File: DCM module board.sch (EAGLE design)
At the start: 2 parts

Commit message: Add files via upload
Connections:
- new net N$1: U$1.+IN
- new net N$3: U$1.-IN
- new net N$4: U$2.+IN
- new net N$5: U$2.-IN
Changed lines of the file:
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@@
 <setting verticaltext="up"/>
 </settings>
-<grid distance="0.1" unitdist="inch" unit="inch" style="lines" multiple="1" display="no" altdistance="0.01" altunitdist="inch" altunit="inch"/>
+<grid distance="1" unitdist="mm" unit="mm" style="lines" multiple="1" display="yes" altdistance="0.01" altunitdist="inch" altunit="mm"/>
 <layers>
 <layer number="1" name="Top" color="4" fill="1" visible="no" active="no"/>
@@
 </plain>
 <instances>
-<instance part="U$1" gate="G$1" x="-27.94" y="0" smashed="yes"/>
-<instance part="U$2" gate="G$1" x="48.26" y="0" smashed="yes"/>
+<instance part="U$1" gate="G$1" x="18.36" y="16.02" smashed="yes"/>
+<instance part="U$2" gate="G$1" x="18.36" y="-22.08" smashed="yes"/>
 </instances>
 <busses>
 </busses>
 <nets>
+<net name="N$1" class="0">
+<segment>
+<pinref part="U$1" gate="G$1" pin="+IN"/>
+<wire x1="-4.83" y1="24.02" x2="-15" y2="24.02" width="0.1524" layer="91"/>
+<wire x1="-15" y1="24.02" x2="-15" y2="24" width="0.1524" layer="91"/>
+</segment>
+</net>
+<net name="N$2" class="0">
+<segment>
+<wire x1="-44" y1="25" x2="-64" y2="25" width="0.1524" layer="91"/>
+</segment>
+</net>
+<net name="N$3" class="0">
+<segment>
+<pinref part="U$1" gate="G$1" pin="-IN"/>
+<wire x1="-4.83" y1="8.02" x2="-15" y2="8.02" width="0.1524" layer="91"/>
+<wire x1="-15" y1="8.02" x2="-15" y2="12" width="0.1524" layer="91"/>
+</segment>
+</net>
+<net name="N$4" class="0">
+<segment>
+<wire x1="-15" y1="8" x2="-48" y2="8" width="0.1524" layer="91"/>
+<wire x1="-48" y1="8" x2="-48" y2="-3" width="0.1524" layer="91"/>
+<pinref part="U$2" gate="G$1" pin="+IN"/>
+<wire x1="-48" y1="-3" x2="-48" y2="-14.08" width="0.1524" layer="91"/>
+<wire x1="-48" y1="-14.08" x2="-4.83" y2="-14.08" width="0.1524" layer="91"/>
+<wire x1="-48" y1="-3" x2="-63" y2="-3" width="0.1524" layer="91"/>
+<junction x="-48" y="-3"/>
+</segment>
+</net>
+<net name="N$5" class="0">
+<segment>
+<pinref part="U$2" gate="G$1" pin="-IN"/>
+<wire x1="-4.83" y1="-30.08" x2="-62" y2="-30.08" width="0.1524" layer="91"/>
+<wire x1="-62" y1="-30.08" x2="-62" y2="-30" width="0.1524" layer="91"/>
+</segment>
+</net>
 </nets>
 </sheet>

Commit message: Add files via upload
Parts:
- added C1, C2: (no value), capacitor-emi:B58035U5305M062
- added R1, R2: (no value), resistor-power:RMG100-H
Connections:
- removed net N$4: U$2.+IN
- new net N$2: C2.2, R2.2, U$2.+IN
- new net N$6: U$1.-OUT1, U$1.-OUT2, U$2.-OUT1, U$2.-OUT2
- new net N$7: R1.1
- new net N$8: U$1.+OUT1, U$1.+OUT2, U$2.+OUT1, U$2.+OUT2
- net N$1: now also C1.2, R1.2
- net N$3: now also C2.1, U$2.-IN; no longer U$1.-IN
- net N$5: now also C1.1, R2.1, U$1.-IN; no longer U$2.-IN
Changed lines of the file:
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@@
 <setting verticaltext="up"/>
 </settings>
-<grid distance="1" unitdist="mm" unit="mm" style="lines" multiple="1" display="yes" altdistance="0.01" altunitdist="inch" altunit="mm"/>
+<grid distance="1" unitdist="mm" unit="mm" style="lines" multiple="1" display="yes" altdistance="0.1" altunitdist="mm" altunit="mm"/>
 <layers>
 <layer number="1" name="Top" color="4" fill="1" visible="no" active="no"/>
@@
 <part name="U$1" library="dc-dc-converter" library_urn="urn:adsk.eagle:library:24542449" deviceset="DCM4623TD2N13C8T00" device="" package3d_urn="urn:adsk.eagle:package:24542464/2"/>
 <part name="U$2" library="dc-dc-converter" library_urn="urn:adsk.eagle:library:24542449" deviceset="DCM4623TD2N13C8T00" device="" package3d_urn="urn:adsk.eagle:package:24542464/2"/>
+<part name="R1" library="resistor-power" library_urn="urn:adsk.eagle:library:344" deviceset="RMG100" device="-H" package3d_urn="urn:adsk.eagle:package:25183/1"/>
+<part name="R2" library="resistor-power" library_urn="urn:adsk.eagle:library:344" deviceset="RMG100" device="-H" package3d_urn="urn:adsk.eagle:package:25183/1"/>
+<part name="C1" library="capacitor-emi" library_urn="urn:adsk.eagle:library:24583833" deviceset="B58035U5305M062" device="" package3d_urn="urn:adsk.eagle:package:24583837/1"/>
+<part name="C2" library="capacitor-emi" library_urn="urn:adsk.eagle:library:24583833" deviceset="B58035U5305M062" device="" package3d_urn="urn:adsk.eagle:package:24583837/1"/>
 </parts>
 <sheets>
@@
 <instance part="U$1" gate="G$1" x="18.36" y="16.02" smashed="yes"/>
 <instance part="U$2" gate="G$1" x="18.36" y="-22.08" smashed="yes"/>
+<instance part="R1" gate="G$1" x="-27" y="30" smashed="yes">
+<attribute name="NAME" x="-30.81" y="31.3716" size="1.778" layer="95"/>
+<attribute name="VALUE" x="-30.81" y="27.079" size="1.778" layer="96"/>
+</instance>
+<instance part="R2" gate="G$1" x="-26" y="-6" smashed="yes">
+<attribute name="NAME" x="-29.81" y="-4.6284" size="1.778" layer="95"/>
+<attribute name="VALUE" x="-29.81" y="-8.921" size="1.778" layer="96"/>
+</instance>
+<instance part="C1" gate="A" x="-15" y="14" smashed="yes" rot="R90">
+<attribute name="VALUE" x="-9.4628" y="8.8438" size="3.4798" layer="96" ratio="10" rot="SR90"/>
+<attribute name="NAME" x="-17.0828" y="9.9106" size="3.4798" layer="95" ratio="10" rot="SR90"/>
+</instance>
+<instance part="C2" gate="A" x="-12" y="-24" smashed="yes" rot="R90">
+<attribute name="VALUE" x="-6.4628" y="-29.1562" size="3.4798" layer="96" ratio="10" rot="SR90"/>
+</instance>
 </instances>
 <busses>
@@
 <pinref part="U$1" gate="G$1" pin="+IN"/>
 <wire x1="-4.83" y1="24.02" x2="-15" y2="24.02" width="0.1524" layer="91"/>
+<wire x1="-15" y1="24.02" x2="-15" y2="30" width="0.1524" layer="91"/>
+<pinref part="R1" gate="G$1" pin="2"/>
+<wire x1="-15" y1="30" x2="-21.92" y2="30" width="0.1524" layer="91"/>
+<pinref part="C1" gate="A" pin="2"/>
 <wire x1="-15" y1="24.02" x2="-15" y2="24" width="0.1524" layer="91"/>
+<wire x1="-15" y1="24" x2="-15" y2="21.62" width="0.1524" layer="91"/>
+<wire x1="-15" y1="24" x2="-22" y2="24" width="0.1524" layer="91"/>
+<junction x="-15" y="24"/>
+</segment>
+</net>
+<net name="N$8" class="0">
+<segment>
+<pinref part="U$2" gate="G$1" pin="+OUT2"/>
+<wire x1="50" y1="24" x2="50" y2="13" width="0.1524" layer="91"/>
+<wire x1="50" y1="13" x2="50" y2="-14" width="0.1524" layer="91"/>
+<wire x1="50" y1="-14" x2="50" y2="-25" width="0.1524" layer="91"/>
+<wire x1="50" y1="-25" x2="41.55" y2="-25" width="0.1524" layer="91"/>
+<wire x1="41.55" y1="-25" x2="41.55" y2="-24.83" width="0.1524" layer="91"/>
+<pinref part="U$2" gate="G$1" pin="+OUT1"/>
+<wire x1="41.55" y1="-13.83" x2="41.55" y2="-14" width="0.1524" layer="91"/>
+<wire x1="41.55" y1="-14" x2="50" y2="-14" width="0.1524" layer="91"/>
+<junction x="50" y="-14"/>
+<pinref part="U$1" gate="G$1" pin="+OUT2"/>
+<wire x1="41.55" y1="13.27" x2="41.55" y2="13" width="0.1524" layer="91"/>
+<wire x1="41.55" y1="13" x2="50" y2="13" width="0.1524" layer="91"/>
+<junction x="50" y="13"/>
+<pinref part="U$1" gate="G$1" pin="+OUT1"/>
+<wire x1="41.55" y1="24.27" x2="41.55" y2="24" width="0.1524" layer="91"/>
+<wire x1="41.55" y1="24" x2="50" y2="24" width="0.1524" layer="91"/>
+<junction x="50" y="24"/>
+<wire x1="50" y1="24" x2="50" y2="40" width="0.1524" layer="91"/>
+</segment>
+</net>
+<net name="N$6" class="0">
+<segment>
+<wire x1="61" y1="-30" x2="61" y2="-19" width="0.1524" layer="91"/>
+<pinref part="U$2" gate="G$1" pin="-OUT2"/>
+<wire x1="61" y1="-19" x2="61" y2="8" width="0.1524" layer="91"/>
+<wire x1="61" y1="8" x2="61" y2="19" width="0.1524" layer="91"/>
+<wire x1="61" y1="19" x2="61" y2="40" width="0.1524" layer="91"/>
+<wire x1="41.55" y1="-30.33" x2="41.55" y2="-30" width="0.1524" layer="91"/>
+<wire x1="41.55" y1="-30" x2="61" y2="-30" width="0.1524" layer="91"/>
+<pinref part="U$2" gate="G$1" pin="-OUT1"/>
+<wire x1="41.55" y1="-19.33" x2="41.55" y2="-19" width="0.1524" layer="91"/>
+<wire x1="41.55" y1="-19" x2="61" y2="-19" width="0.1524" layer="91"/>
+<junction x="61" y="-19"/>
+<pinref part="U$1" gate="G$1" pin="-OUT2"/>
+<wire x1="41.55" y1="7.77" x2="41.55" y2="8" width="0.1524" layer="91"/>
+<wire x1="41.55" y1="8" x2="61" y2="8" width="0.1524" layer="91"/>
+<junction x="61" y="8"/>
+<pinref part="U$1" gate="G$1" pin="-OUT1"/>
+<wire x1="41.55" y1="18.77" x2="41.55" y2="19" width="0.1524" layer="91"/>
+<wire x1="41.55" y1="19" x2="61" y2="19" width="0.1524" layer="91"/>
+<junction x="61" y="19"/>
 </segment>
 </net>
 <net name="N$2" class="0">
 <segment>
-<wire x1="-44" y1="25" x2="-64" y2="25" width="0.1524" layer="91"/>
+<pinref part="U$2" gate="G$1" pin="+IN"/>
+<wire x1="-4.83" y1="-14.08" x2="-5" y2="-14.08" width="0.1524" layer="91"/>
+<wire x1="-5" y1="-14.08" x2="-5" y2="-13" width="0.1524" layer="91"/>
+<wire x1="-5" y1="-13" x2="-12" y2="-13" width="0.1524" layer="91"/>
+<pinref part="C2" gate="A" pin="2"/>
+<wire x1="-12" y1="-13" x2="-12" y2="-16.38" width="0.1524" layer="91"/>
+<junction x="-12" y="-13"/>
+<pinref part="R2" gate="G$1" pin="2"/>
+<wire x1="-12" y1="-13" x2="-12" y2="-6" width="0.1524" layer="91"/>
+<wire x1="-12" y1="-6" x2="-20.92" y2="-6" width="0.1524" layer="91"/>
+</segment>
+</net>
+<net name="N$5" class="0">
+<segment>
+<pinref part="U$1" gate="G$1" pin="-IN"/>
+<wire x1="-4.83" y1="8.02" x2="-5" y2="8.02" width="0.1524" layer="91"/>
+<wire x1="-5" y1="8.02" x2="-5" y2="7" width="0.1524" layer="91"/>
+<wire x1="-5" y1="7" x2="-15" y2="7" width="0.1524" layer="91"/>
+<pinref part="C1" gate="A" pin="1"/>
+<wire x1="-15" y1="7" x2="-15" y2="14" width="0.1524" layer="91"/>
+<wire x1="-15" y1="7" x2="-42" y2="7" width="0.1524" layer="91"/>
+<junction x="-15" y="7"/>
+<wire x1="-42" y1="7" x2="-42" y2="-2" width="0.1524" layer="91"/>
+<wire x1="-42" y1="-2" x2="-42" y2="-13" width="0.1524" layer="91"/>
+<wire x1="-36" y1="-13" x2="-31" y2="-13" width="0.1524" layer="91"/>
+<wire x1="-36" y1="-6" x2="-36" y2="-13" width="0.1524" layer="91"/>
+<pinref part="R2" gate="G$1" pin="1"/>
+<wire x1="-31.08" y1="-6" x2="-36" y2="-6" width="0.1524" layer="91"/>
+<wire x1="-42" y1="-13" x2="-36" y2="-13" width="0.1524" layer="91"/>
+<junction x="-36" y="-13"/>
+<wire x1="-42" y1="-2" x2="-59" y2="-2" width="0.1524" layer="91"/>
+<junction x="-42" y="-2"/>
+</segment>
+</net>
+<net name="N$7" class="0">
+<segment>
+<pinref part="R1" gate="G$1" pin="1"/>
+<wire x1="-32.08" y1="30" x2="-39" y2="30" width="0.1524" layer="91"/>
+<wire x1="-39" y1="30" x2="-39" y2="24" width="0.1524" layer="91"/>
+<wire x1="-32" y1="24" x2="-39" y2="24" width="0.1524" layer="91"/>
+<wire x1="-39" y1="24" x2="-60" y2="24" width="0.1524" layer="91"/>
+<junction x="-39" y="24"/>
 </segment>
 </net>
 <net name="N$3" class="0">
 <segment>
-<pinref part="U$1" gate="G$1" pin="-IN"/>
-<wire x1="-4.83" y1="8.02" x2="-15" y2="8.02" width="0.1524" layer="91"/>
-<wire x1="-15" y1="8.02" x2="-15" y2="12" width="0.1524" layer="91"/>
-</segment>
-</net>
-<net name="N$4" class="0">
-<segment>
-<wire x1="-15" y1="8" x2="-48" y2="8" width="0.1524" layer="91"/>
-<wire x1="-48" y1="8" x2="-48" y2="-3" width="0.1524" layer="91"/>
-<pinref part="U$2" gate="G$1" pin="+IN"/>
-<wire x1="-48" y1="-3" x2="-48" y2="-14.08" width="0.1524" layer="91"/>
-<wire x1="-48" y1="-14.08" x2="-4.83" y2="-14.08" width="0.1524" layer="91"/>
-<wire x1="-48" y1="-3" x2="-63" y2="-3" width="0.1524" layer="91"/>
-<junction x="-48" y="-3"/>
-</segment>
-</net>
-<net name="N$5" class="0">
-<segment>
 <pinref part="U$2" gate="G$1" pin="-IN"/>
-<wire x1="-4.83" y1="-30.08" x2="-62" y2="-30.08" width="0.1524" layer="91"/>
-<wire x1="-62" y1="-30.08" x2="-62" y2="-30" width="0.1524" layer="91"/>
-</segment>
-</net>
+<wire x1="-4.83" y1="-30.08" x2="-5" y2="-30.08" width="0.1524" layer="91"/>
+<wire x1="-5" y1="-30.08" x2="-5" y2="-31" width="0.1524" layer="91"/>
+<wire x1="-5" y1="-31" x2="-12" y2="-31" width="0.1524" layer="91"/>
+<pinref part="C2" gate="A" pin="1"/>
+<wire x1="-12" y1="-31" x2="-12" y2="-24" width="0.1524" layer="91"/>
+<junction x="-12" y="-31"/>
+<wire x1="-12" y1="-31" x2="-58" y2="-31" width="0.1524" layer="91"/>
+</segment>
+</net>

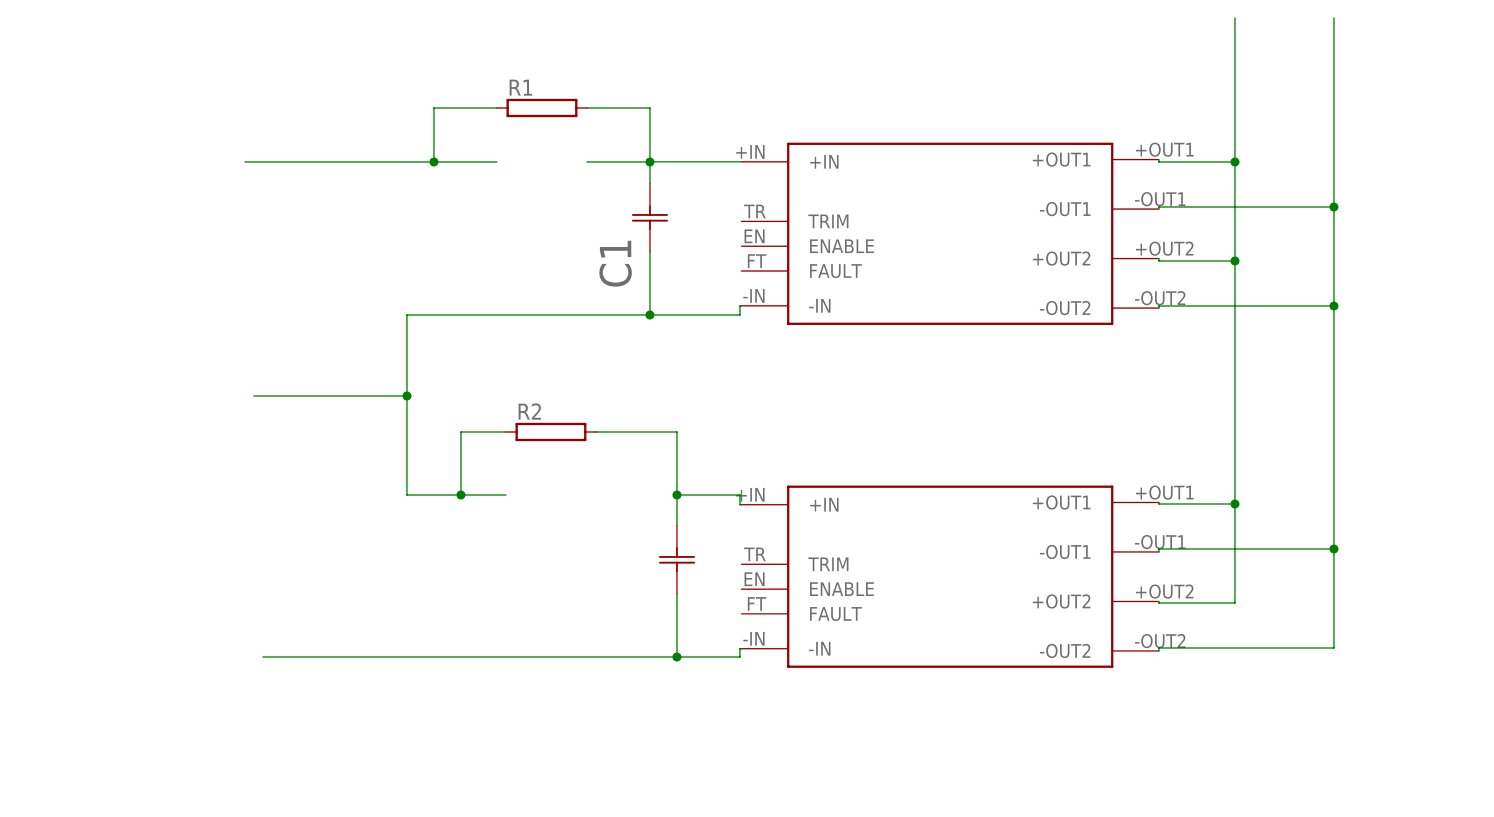
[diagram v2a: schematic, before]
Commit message: Add files via upload
0.9V
To add - FT circuit, TR circuit
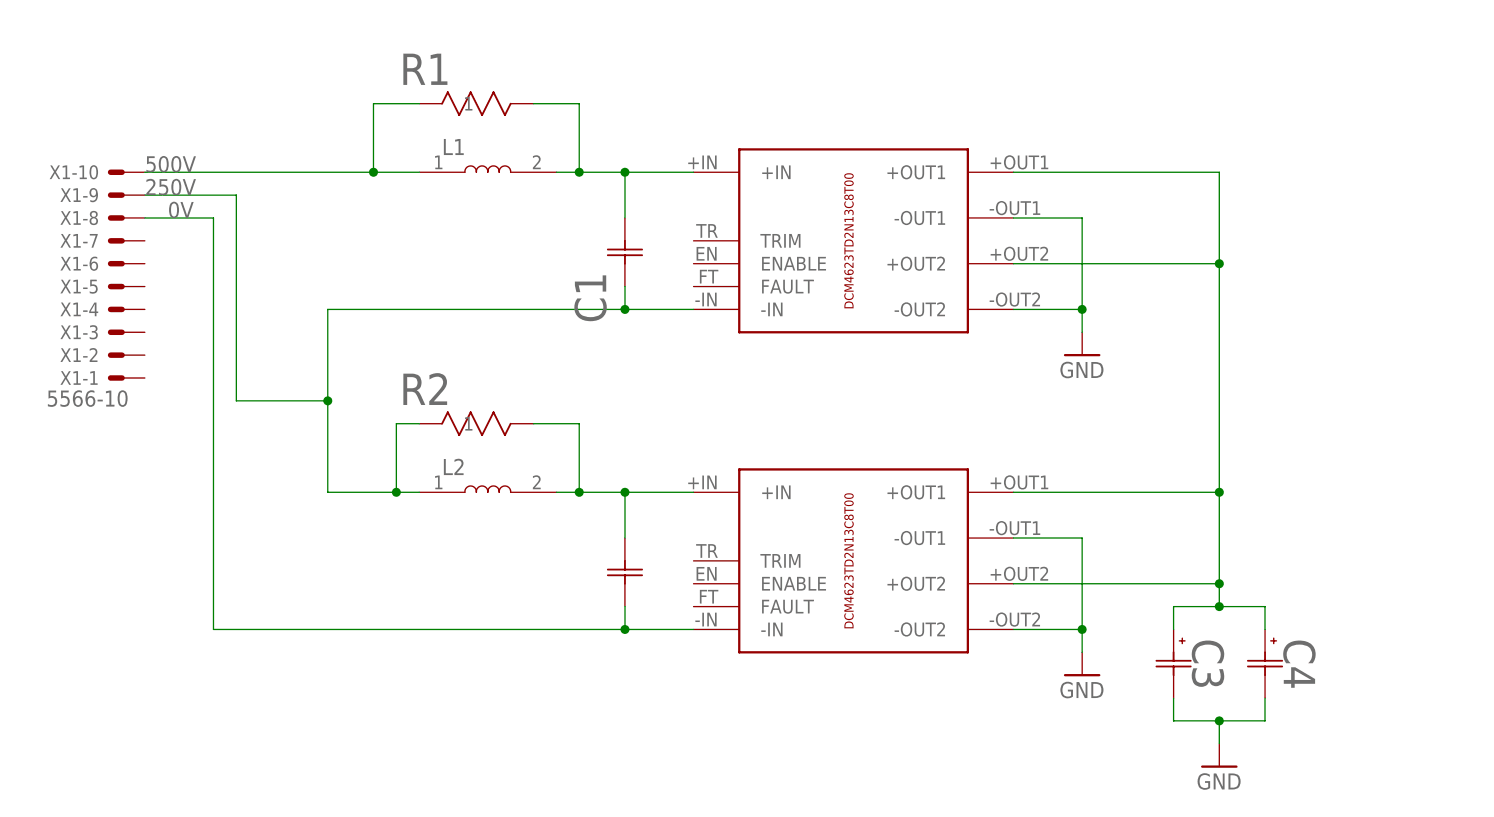
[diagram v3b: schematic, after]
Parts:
- added C3, C4: UBY1E472MHL1TN, Nichicon:UBY1E472MHL1TN
- added L1, L2: SRP1265A-330M, SRP1265A-330M:SRP1265A-330M
- added X1: 5566-10, con-molex:5566-10
- R1, R2: value (none) -> TEH100M2R50FE; device resistor-power:RMG100-H -> TEH100M2R50FE:TEH100M2R50FE
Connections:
- removed net N$2: C2.2, R2.2, U$2.+IN
- removed net N$5: C1.1, R2.1, U$1.-IN
- removed net N$6: U$1.-OUT1, U$1.-OUT2, U$2.-OUT1, U$2.-OUT2
- removed net N$7: R1.1
- removed net N$8: U$1.+OUT1, U$1.+OUT2, U$2.+OUT1, U$2.+OUT2
- new net 0V: C2.1, U$2.-IN, X1-8.S
- new net 250V: C1.1, L2.1, R2.1, U$1.-IN, X1-9.S
- new net 500V: L1.1, R1.1, X1-10.S
- new net GND: C3.2, C4.2, U$1.-OUT1, U$1.-OUT2, U$2.-OUT1, U$2.-OUT2
- new net N$4: C2.2, L2.2, R2.2, U$2.+IN
- net N$1: now also L1.2
- net N$3: now also C3.1, C4.1, U$1.+OUT1, U$1.+OUT2, U$2.+OUT1, U$2.+OUT2; no longer C2.1, U$2.-IN
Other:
- moved on the sheet: C1
